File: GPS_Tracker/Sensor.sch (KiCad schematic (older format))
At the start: 2 parts

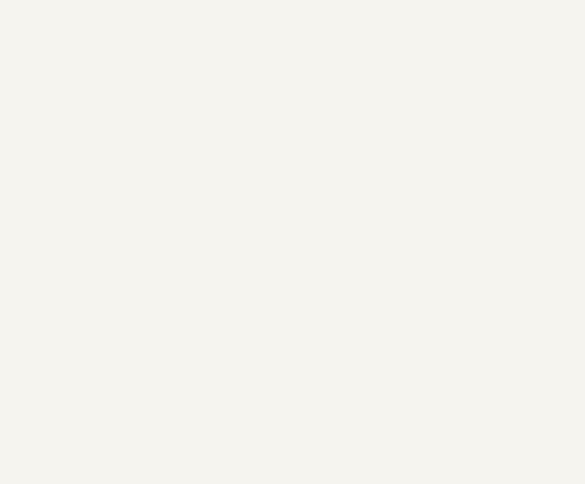
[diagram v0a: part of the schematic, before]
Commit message: added datasheets and worked on artemis module"
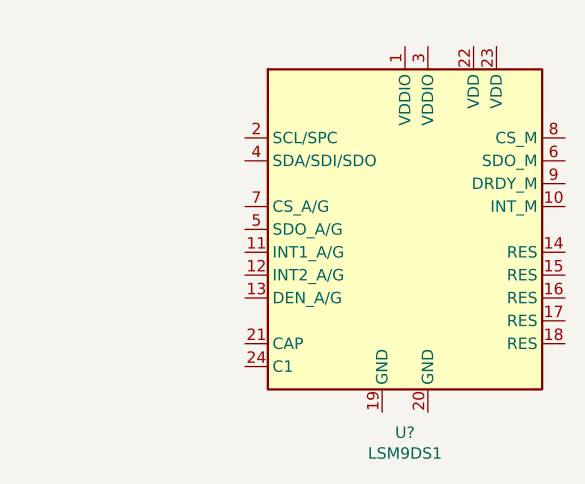
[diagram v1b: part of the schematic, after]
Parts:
- added U?: LSM9DS1, Package_LGA:LGA-24L_3x3.5mm_P0.43mm, symbol Sensor_Motion:LSM9DS1
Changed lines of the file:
@@
 $Descr A4 11693 8268
 encoding utf-8
-Sheet 1 6
+Sheet 1 7
 Title ""
 Date ""
@@
 Wire Wire Line
 	2450 2350 2450 2200
+$Comp
+L Sensor_Motion:LSM9DS1 U?
+U 1 1 5E729015
+P 7650 2900
+F 0 "U?" H 7650 2011 50  0000 C CNN
+F 1 "LSM9DS1" H 7650 1920 50  0000 C CNN
+F 2 "Package_LGA:LGA-24L_3x3.5mm_P0.43mm" H 9150 3650 50  0001 C CNN
+F 3 "http://www.st.com/content/ccc/resource/technical/document/datasheet/1e/3f/2a/d6/25/eb/48/46/DM00103319.pdf/files/DM00103319.pdf/jcr:content/translations/en.DM00103319.pdf" H 7650 3000 50  0001 C CNN
+	1    7650 2900
+	1    0    0    -1
+$EndComp
 $EndSCHEMATC

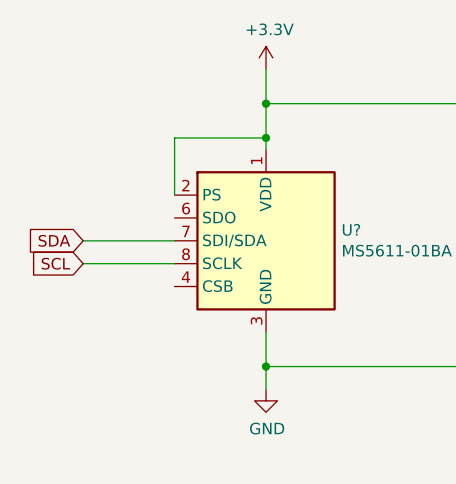
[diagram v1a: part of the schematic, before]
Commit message: added hichary labels
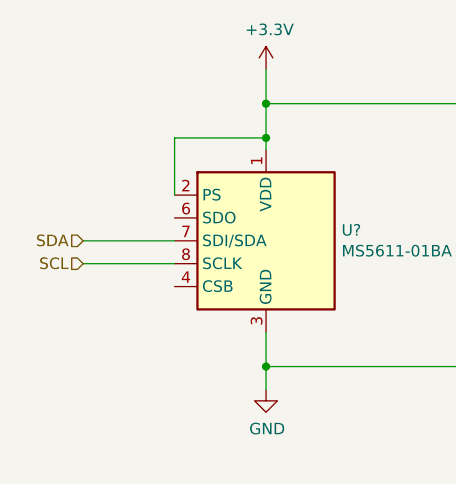
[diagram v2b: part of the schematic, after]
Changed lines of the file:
@@
 	1    0    0    -1
 $EndComp
-Text GLabel 1650 3050 0    50   Input ~ 0
-SCL
-Text GLabel 1650 2950 0    50   Input ~ 0
-SDA
 Wire Wire Line
 	1650 3050 2050 3050
@@
 	1    0    0    -1
 $EndComp
+Text HLabel 1650 3050 0    50   Input ~ 0
+SCL
+Text HLabel 1650 2950 0    50   Input ~ 0
+SDA
 $EndSCHEMATC

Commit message: started 9dof
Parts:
- removed U?: LSM9DS1, Package_LGA:LGA-24L_3x3.5mm_P0.43mm, symbol Sensor_Motion:LSM9DS1
- added C? (x2): 0.1uF, symbol pspice:CAP
- added C?: CAP, symbol pspice:CAP
- added U?: ICM-20948, Sensor_Motion:InvenSense_QFN-24_3x3mm_P0.4mm, symbol Sensor_Motion:ICM-20948
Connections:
- net +3V3: now also C?.2, C?.2, U?.13 (VDD), U?.8 (VDDIO)
- net GND: now also C?.1, C?.1, U?.18 (GND), U?.20 (GND)
- new net: C?.2, U?.10 (REGOUT)
- new net SCLK: U?.23 (SCL/SCLK)
- new net SDI: U?.24 (SDA/SDI)
- new net nCS: U?.22 (~CS)
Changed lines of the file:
@@
 $Descr A4 11693 8268
 encoding utf-8
-Sheet 1 7
+Sheet 1 1
 Title ""
 Date ""
@@
 Wire Wire Line
 	2450 2350 2450 2200
-$Comp
-L Sensor_Motion:LSM9DS1 U?
-U 1 1 5E729015
-P 7650 2900
-F 0 "U?" H 7650 2011 50  0000 C CNN
-F 1 "LSM9DS1" H 7650 1920 50  0000 C CNN
-F 2 "Package_LGA:LGA-24L_3x3.5mm_P0.43mm" H 9150 3650 50  0001 C CNN
-F 3 "http://www.st.com/content/ccc/resource/technical/document/datasheet/1e/3f/2a/d6/25/eb/48/46/DM00103319.pdf/files/DM00103319.pdf/jcr:content/translations/en.DM00103319.pdf" H 7650 3000 50  0001 C CNN
-	1    7650 2900
-	1    0    0    -1
-$EndComp
 Text HLabel 1650 3050 0    50   Input ~ 0
 SCL
 Text HLabel 1650 2950 0    50   Input ~ 0
 SDA
+$Comp
+L Sensor_Motion:ICM-20948 U?
+U 1 1 5E72C53E
+P 7600 3250
+F 0 "U?" H 7600 2461 50  0000 C CNN
+F 1 "ICM-20948" H 7600 2370 50  0000 C CNN
+F 2 "Sensor_Motion:InvenSense_QFN-24_3x3mm_P0.4mm" H 7600 2250 50  0001 C CNN
+F 3 "http://www.invensense.com/wp-content/uploads/2016/06/DS-000189-ICM-20948-v1.3.pdf" H 7600 3100 50  0001 C CNN
+	1    7600 3250
+	1    0    0    -1
+$EndComp
+$Comp
+L power:GND #PWR?
+U 1 1 5E72EA31
+P 7600 4300
+F 0 "#PWR?" H 7600 4050 50  0001 C CNN
+F 1 "GND" H 7605 4127 50  0000 C CNN
+F 2 "" H 7600 4300 50  0001 C CNN
+F 3 "" H 7600 4300 50  0001 C CNN
+	1    7600 4300
+	1    0    0    -1
+$EndComp
+Wire Wire Line
+	7600 3950 7600 4300
+Text GLabel 6900 3050 0    50   Input ~ 0
+SDI
+Text GLabel 6900 3150 0    50   Input ~ 0
+SCLK
+Text GLabel 6900 3250 0    50   Input ~ 0
+nCS
+Wire Wire Line
+	6900 3050 7100 3050
+Wire Wire Line
+	6900 3150 7100 3150
+Wire Wire Line
+	6900 3250 7100 3250
+$Comp
+L power:GND #PWR?
+U 1 1 5E7302D3
+P 8300 2400
+F 0 "#PWR?" H 8300 2150 50  0001 C CNN
+F 1 "GND" H 8305 2227 50  0000 C CNN
+F 2 "" H 8300 2400 50  0001 C CNN
+F 3 "" H 8300 2400 50  0001 C CNN
+	1    8300 2400
+	0    -1   -1   0
+$EndComp
+$Comp
+L power:GND #PWR?
+U 1 1 5E730942
+P 6900 2400
+F 0 "#PWR?" H 6900 2150 50  0001 C CNN
+F 1 "GND" H 6905 2227 50  0000 C CNN
+F 2 "" H 6900 2400 50  0001 C CNN
+F 3 "" H 6900 2400 50  0001 C CNN
+	1    6900 2400
+	0    1    1    0
+$EndComp
+$Comp
+L pspice:CAP C?
+U 1 1 5E731644
+P 7250 2400
+F 0 "C?" V 7565 2400 50  0000 C CNN
+F 1 "0.1uF" V 7474 2400 50  0000 C CNN
+F 2 "" H 7250 2400 50  0001 C CNN
+F 3 "~" H 7250 2400 50  0001 C CNN
+	1    7250 2400
+	0    -1   -1   0
+$EndComp
+$Comp
+L pspice:CAP C?
+U 1 1 5E731D9C
+P 7950 2400
+F 0 "C?" H 8128 2446 50  0000 L CNN
+F 1 "CAP" H 8128 2355 50  0000 L CNN
+F 2 "" H 7950 2400 50  0001 C CNN
+F 3 "~" H 7950 2400 50  0001 C CNN
+	1    7950 2400
+	0    1    1    0
+$EndComp
+$Comp
+L power:+3.3V #PWR?
+U 1 1 5E733708
+P 7500 2300
+F 0 "#PWR?" H 7500 2150 50  0001 C CNN
+F 1 "+3.3V" H 7515 2473 50  0000 C CNN
+F 2 "" H 7500 2300 50  0001 C CNN
+F 3 "" H 7500 2300 50  0001 C CNN
+	1    7500 2300
+	1    0    0    -1
+$EndComp
+$Comp
+L power:+3.3V #PWR?
+U 1 1 5E733BE9
+P 7700 2300
+F 0 "#PWR?" H 7700 2150 50  0001 C CNN
+F 1 "+3.3V" H 7715 2473 50  0000 C CNN
+F 2 "" H 7700 2300 50  0001 C CNN
+F 3 "" H 7700 2300 50  0001 C CNN
+	1    7700 2300
+	1    0    0    -1
+$EndComp
+Wire Wire Line
+	7500 2300 7500 2400
+Wire Wire Line
+	7700 2300 7700 2400
+Connection ~ 7500 2400
+Wire Wire Line
+	7500 2400 7500 2550
+Connection ~ 7700 2400
+Wire Wire Line
+	7700 2400 7700 2550
+Wire Wire Line
+	8200 2400 8300 2400
+$Comp
+L pspice:CAP C?
+U 1 1 5E73B2C6
+P 8500 3450
+F 0 "C?" V 8185 3450 50  0000 C CNN
+F 1 "0.1uF" V 8276 3450 50  0000 C CNN
+F 2 "" H 8500 3450 50  0001 C CNN
+F 3 "~" H 8500 3450 50  0001 C CNN
+	1    8500 3450
+	0    1    1    0
+$EndComp
+$Comp
+L power:GND #PWR?
+U 1 1 5E73BEE0
+P 8950 3450
+F 0 "#PWR?" H 8950 3200 50  0001 C CNN
+F 1 "GND" V 8955 3322 50  0000 R CNN
+F 2 "" H 8950 3450 50  0001 C CNN
+F 3 "" H 8950 3450 50  0001 C CNN
+	1    8950 3450
+	0    -1   -1   0
+$EndComp
+Wire Wire Line
+	8100 3450 8250 3450
+Wire Wire Line
+	8750 3450 8950 3450
 $EndSCHEMATC
